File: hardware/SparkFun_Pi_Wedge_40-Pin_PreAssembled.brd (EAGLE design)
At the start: 82.5 x 65.5 mm, 17 parts

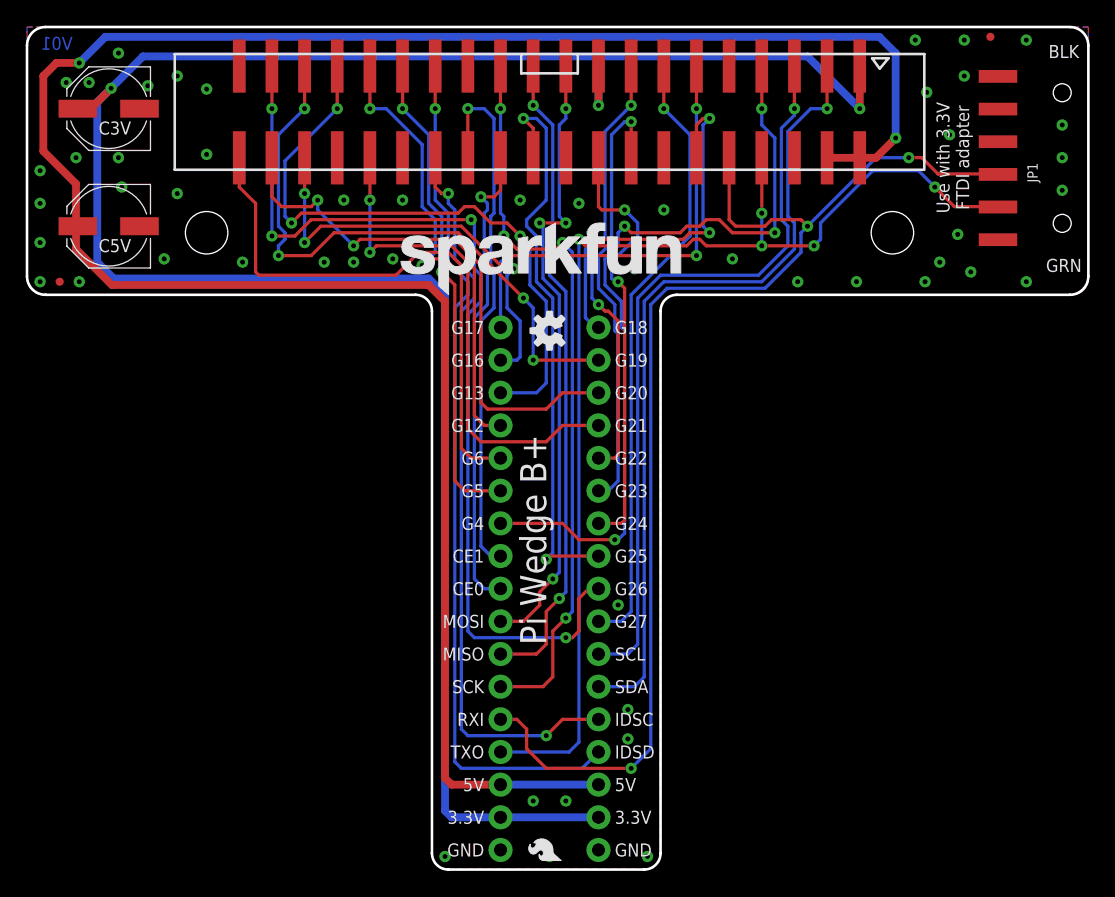
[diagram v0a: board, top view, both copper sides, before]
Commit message: Updates after group review.
A few silk touch-ups.
Renaming to "Pi Wedge 40-Pin".
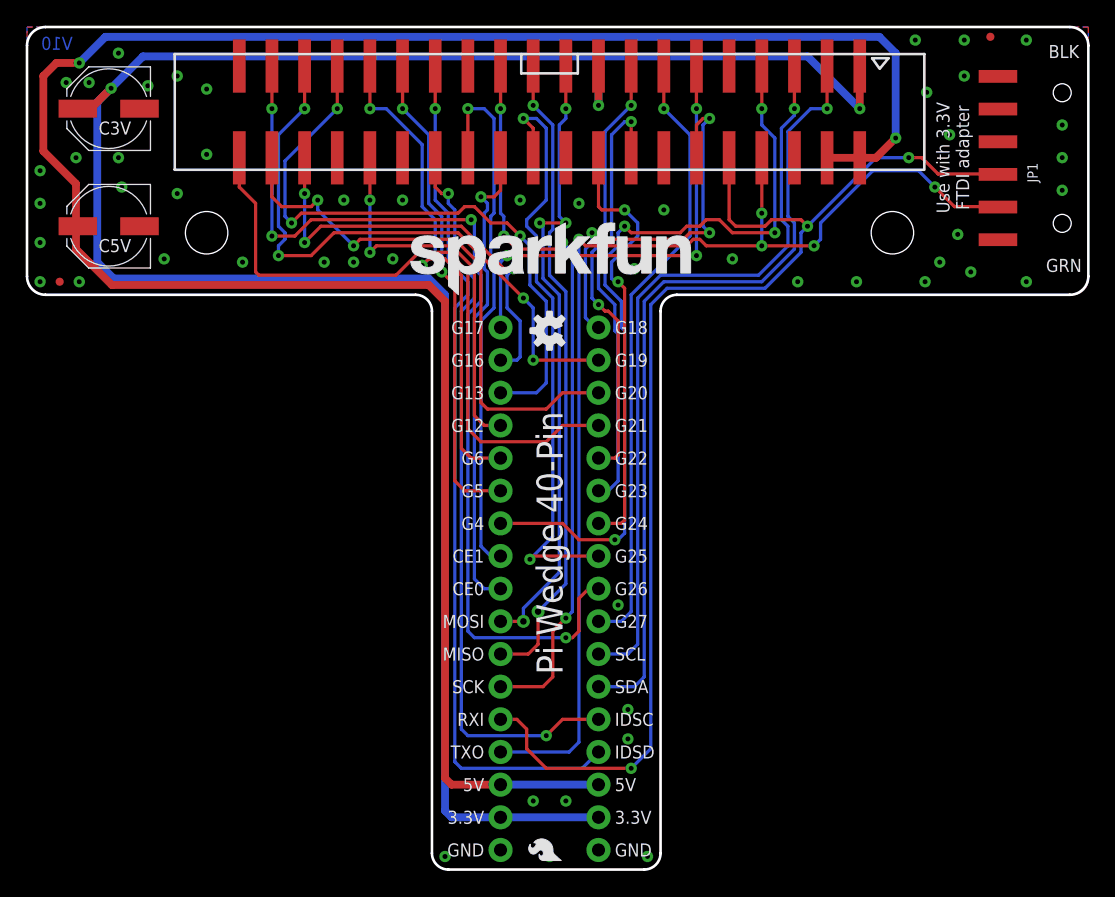
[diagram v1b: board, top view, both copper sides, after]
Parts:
- moved LOGO1 0.76 mm to (29.8, 44.7)
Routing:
- net GP25: track 44.9 -> 46.6 mm
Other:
- board text added: "Pi Wedge 40-Pin"
- board text added: "V10"
- board text removed: "Pi Wedge B+"
- board text removed: "V01"
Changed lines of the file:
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@@
 <wire x1="48.006" y1="0" x2="49.276" y2="1.27" width="0.2032" layer="20" curve="90"/>
 <wire x1="49.276" y1="1.27" x2="49.276" y2="43.434" width="0.2032" layer="20"/>
-<text x="3.556" y="63.754" size="1.016" layer="16" font="vector" ratio="20" rot="SMR0">V01</text>
+<text x="3.556" y="63.754" size="1.016" layer="16" font="vector" ratio="20" rot="SMR0">V10</text>
 <text x="35.56" y="1.524" size="1.016" layer="21" font="vector" ratio="19" rot="SR0" align="center-right">GND</text>
-<text x="40.386" y="25.654" size="2.032" layer="21" font="vector" ratio="19" rot="SR90" align="bottom-center">Pi Wedge B+</text>
+<text x="40.64" y="25.4" size="2.032" layer="21" font="vector" ratio="19" rot="SR90" align="center">Pi Wedge 40-Pin</text>
 <text x="45.72" y="16.764" size="1.016" layer="21" font="vector" ratio="19" rot="SR0" align="center-left">SCL</text>
 <text x="45.72" y="14.224" size="1.016" layer="21" font="vector" ratio="19" rot="SR0" align="center-left">SDA</text>
@@
 <text x="88.9" y="33.02" size="1.778" layer="47" font="vector" ratio="15">2x 0.13" holes
 Clear 4-40 screws</text>
+<text x="40.64" y="25.4" size="2.032" layer="22" font="vector" ratio="19" rot="SMR90" align="center">Pi Wedge 40-Pin</text>
+<text x="80.645" y="46.482" size="1.016" layer="22" font="vector" ratio="19" rot="SMR0" align="bottom-center">GRN</text>
+<text x="80.645" y="63.119" size="1.016" layer="22" font="vector" ratio="19" rot="SMR0" align="bottom-center">BLK</text>
+<text x="78.74" y="55.372" size="1.016" layer="22" font="vector" ratio="19" rot="SMR270" align="bottom-center">Use with 3.3V
+FTDI adapter</text>
 </plain>
 <attributes>
@@
 </element>
 <element name="FRAME2" library="SparkFun-Aesthetics" package="CREATIVE_COMMONS" value="FRAME-LETTER" x="19.558" y="-17.78"/>
-<element name="LOGO1" library="SparkFun-Aesthetics" package="SFE_LOGO_NAME_.2" value="SFE_LOGO_NAME.2_INCH" x="29.083" y="44.704"/>
+<element name="LOGO1" library="SparkFun-Aesthetics" package="SFE_LOGO_NAME_.2" value="SFE_LOGO_NAME.2_INCH" x="29.845" y="44.704"/>
 <element name="STANDOFF1" library="SparkFun-Electromechanical" package="STAND-OFF" value="STAND-OFF" x="13.97" y="49.53"/>
 <element name="STANDOFF2" library="SparkFun-Electromechanical" package="STAND-OFF" value="STAND-OFF" x="67.31" y="49.53"/>
@@
 <contactref element="JP4" pad="10"/>
 <contactref element="JP2" pad="22"/>
-<wire x1="44.45" y1="24.384" x2="40.64" y2="24.384" width="0.254" layer="1"/>
-<wire x1="40.64" y1="24.384" x2="40.386" y2="24.13" width="0.254" layer="1"/>
-<via x="40.386" y="24.13" extent="1-16" drill="0.381"/>
-<wire x1="40.386" y1="24.13" x2="40.894" y2="24.638" width="0.254" layer="16"/>
-<wire x1="40.894" y1="24.638" x2="40.894" y2="44.45" width="0.254" layer="16"/>
+<wire x1="44.45" y1="24.384" x2="39.37" y2="24.384" width="0.254" layer="1"/>
+<wire x1="39.37" y1="24.384" x2="39.116" y2="24.13" width="0.254" layer="1"/>
+<via x="39.116" y="24.13" extent="1-16" drill="0.381"/>
+<wire x1="39.116" y1="24.13" x2="40.894" y2="25.908" width="0.254" layer="16"/>
+<wire x1="40.894" y1="25.908" x2="40.894" y2="44.45" width="0.254" layer="16"/>
 <wire x1="40.894" y1="44.45" x2="39.624" y2="45.72" width="0.254" layer="16"/>
 <wire x1="39.624" y1="49.276" x2="38.862" y2="50.038" width="0.254" layer="16"/>
@@
 <contactref element="JP2" pad="21"/>
 <contactref element="JP3" pad="7"/>
-<wire x1="36.83" y1="16.764" x2="39.624" y2="16.764" width="0.254" layer="1"/>
-<wire x1="39.624" y1="16.764" x2="40.386" y2="17.526" width="0.254" layer="1"/>
-<wire x1="40.386" y1="17.526" x2="40.386" y2="20.066" width="0.254" layer="1"/>
-<wire x1="40.386" y1="20.066" x2="41.402" y2="21.082" width="0.254" layer="1"/>
-<via x="41.402" y="21.082" extent="1-16" drill="0.381"/>
-<wire x1="41.402" y1="21.082" x2="41.91" y2="21.59" width="0.254" layer="16"/>
-<wire x1="41.91" y1="21.59" x2="41.91" y2="44.958" width="0.254" layer="16"/>
+<wire x1="36.83" y1="16.764" x2="38.989" y2="16.764" width="0.254" layer="1"/>
+<wire x1="38.989" y1="16.764" x2="39.751" y2="17.526" width="0.254" layer="1"/>
+<wire x1="39.751" y1="17.526" x2="39.751" y2="20.066" width="0.254" layer="1"/>
+<wire x1="39.751" y1="20.066" x2="41.91" y2="22.225" width="0.254" layer="16"/>
+<wire x1="41.91" y1="22.225" x2="41.91" y2="44.958" width="0.254" layer="16"/>
 <wire x1="41.91" y1="44.958" x2="40.64" y2="46.228" width="0.254" layer="16"/>
 <wire x1="40.64" y1="49.53" x2="40.894" y2="49.784" width="0.254" layer="16"/>
@@
 <via x="39.37" y="59.436" extent="1-16" drill="0.381"/>
 <wire x1="39.37" y1="59.436" x2="40.894" y2="57.912" width="0.254" layer="16"/>
+<via x="39.751" y="20.066" extent="1-16" drill="0.508"/>
 </signal>
 <signal name="MOSI">
@@
 <contactref element="JP3" pad="8"/>
 <wire x1="36.83" y1="19.304" x2="38.608" y2="19.304" width="0.254" layer="1"/>
-<wire x1="38.608" y1="19.304" x2="39.878" y2="20.574" width="0.254" layer="1"/>
-<wire x1="39.878" y1="20.574" x2="39.878" y2="21.59" width="0.254" layer="1"/>
-<wire x1="39.878" y1="21.59" x2="40.894" y2="22.606" width="0.254" layer="1"/>
-<via x="40.894" y="22.606" extent="1-16" drill="0.381"/>
-<wire x1="40.894" y1="22.606" x2="41.402" y2="23.114" width="0.254" layer="16"/>
+<wire x1="38.608" y1="19.304" x2="38.608" y2="20.32" width="0.254" layer="16"/>
+<wire x1="38.608" y1="20.32" x2="41.402" y2="23.114" width="0.254" layer="16"/>
 <wire x1="41.402" y1="23.114" x2="41.402" y2="44.704" width="0.254" layer="16"/>
 <wire x1="41.402" y1="44.704" x2="40.132" y2="45.974" width="0.254" layer="16"/>
@@
 <wire x1="41.91" y1="58.42" x2="41.402" y2="57.912" width="0.254" layer="16"/>
 <wire x1="41.91" y1="59.182" x2="41.91" y2="58.42" width="0.254" layer="16"/>
+<via x="38.608" y="19.304" extent="1-16" drill="0.508"/>
 </signal>
 <signal name="CE0">

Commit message: Updates after checklist review.
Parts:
- JP2: value RASPBERRYPI-B+-GPIO-SMT -> RASPBERRYPI-40-PIN-GPIO-SMT
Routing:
- net 5V: track 175.5 -> 181.2 mm
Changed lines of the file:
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@@
 <setting verticaltext="up"/>
 </settings>
-<grid distance="0.05" unitdist="inch" unit="inch" style="lines" multiple="1" display="yes" altdistance="0.005" altunitdist="inch" altunit="inch"/>
+<grid distance="0.1" unitdist="inch" unit="inch" style="lines" multiple="1" display="yes" altdistance="0.01" altunitdist="inch" altunit="inch"/>
 <layers>
 <layer number="1" name="Top" color="4" fill="1" visible="yes" active="yes"/>
@@
 <layer number="37" name="tTest" color="7" fill="1" visible="no" active="yes"/>
 <layer number="38" name="bTest" color="7" fill="1" visible="no" active="yes"/>
-<layer number="39" name="tKeepout" color="4" fill="11" visible="no" active="yes"/>
+<layer number="39" name="tKeepout" color="4" fill="11" visible="yes" active="yes"/>
 <layer number="40" name="bKeepout" color="1" fill="11" visible="no" active="yes"/>
 <layer number="41" name="tRestrict" color="4" fill="10" visible="no" active="yes"/>
@@
 </element>
 <element name="U$2" library="SparkFun-Aesthetics" package="BREADBOARD_SPACING" value="BREADBOARD_PATTERN" x="40.64" y="68.834"/>
-<element name="JP2" library="SparkFun-Boards" package="2X20-SHROUDED-SMT" value="RASPBERRYPI-B+-GPIO-SMT" x="40.64" y="58.928" rot="R270">
+<element name="JP2" library="SparkFun-Boards" package="2X20-SHROUDED-SMT" value="RASPBERRYPI-40-PIN-GPIO-SMT" x="40.64" y="58.928" rot="R270">
 <attribute name="PROD_ID" value="CONN-13143" x="40.64" y="58.928" size="1.778" layer="27" rot="R270" display="off"/>
 </element>
@@
 <via x="67.564" y="56.896" extent="1-16" drill="0.381"/>
 <wire x1="3.81" y1="50.038" x2="3.95" y2="50.038" width="0.6096" layer="1"/>
-<wire x1="62.23" y1="55.3593" x2="64.77" y2="55.3593" width="0.6096" layer="1"/>
+<wire x1="62.23" y1="55.3593" x2="62.23" y2="52.832" width="0.6096" layer="1"/>
+<wire x1="62.23" y1="52.832" x2="62.992" y2="52.07" width="0.6096" layer="1"/>
+<wire x1="62.992" y1="52.07" x2="64.008" y2="52.07" width="0.6096" layer="1"/>
+<wire x1="64.008" y1="52.07" x2="64.77" y2="52.832" width="0.6096" layer="1"/>
+<wire x1="64.77" y1="52.832" x2="64.77" y2="55.3593" width="0.6096" layer="1"/>
 <wire x1="64.77" y1="55.3593" x2="66.0273" y2="55.3593" width="0.6096" layer="1"/>
 <wire x1="66.0273" y1="55.3593" x2="67.564" y2="56.896" width="0.6096" layer="1"/>

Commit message: Updating caps values.
It had 47uf library parts (CAP-10547), but the schem incorrectly showed
10uf as the value.

Schem now reads 47uf.
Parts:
- C3V, C5V: value 10uf -> 47uf
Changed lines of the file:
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@@
 <setting verticaltext="up"/>
 </settings>
-<grid distance="0.1" unitdist="inch" unit="inch" style="lines" multiple="1" display="yes" altdistance="0.01" altunitdist="inch" altunit="inch"/>
+<grid distance="0.05" unitdist="inch" unit="inch" style="lines" multiple="1" display="yes" altdistance="0.005" altunitdist="inch" altunit="inch"/>
 <layers>
 <layer number="1" name="Top" color="4" fill="1" visible="yes" active="yes"/>
@@
 <layer number="37" name="tTest" color="7" fill="1" visible="no" active="yes"/>
 <layer number="38" name="bTest" color="7" fill="1" visible="no" active="yes"/>
-<layer number="39" name="tKeepout" color="4" fill="11" visible="yes" active="yes"/>
+<layer number="39" name="tKeepout" color="4" fill="11" visible="no" active="yes"/>
 <layer number="40" name="bKeepout" color="1" fill="11" visible="no" active="yes"/>
 <layer number="41" name="tRestrict" color="4" fill="10" visible="no" active="yes"/>
@@
 <element name="STANDOFF1" library="SparkFun-Electromechanical" package="STAND-OFF" value="STAND-OFF" x="13.97" y="49.53"/>
 <element name="STANDOFF2" library="SparkFun-Electromechanical" package="STAND-OFF" value="STAND-OFF" x="67.31" y="49.53"/>
-<element name="C5V" library="SparkFun-Capacitors" package="PANASONIC_D" value="10uf" x="6.35" y="50.038" rot="R180">
+<element name="C5V" library="SparkFun-Capacitors" package="PANASONIC_D" value="47uf" x="6.35" y="50.038" rot="R180">
 <attribute name="PROD_ID" value="CAP-10547" x="6.35" y="50.038" size="1.778" layer="27" rot="R180" display="off"/>
 </element>
-<element name="C3V" library="SparkFun-Capacitors" package="PANASONIC_D" value="10uf" x="6.35" y="59.182" rot="R180">
+<element name="C3V" library="SparkFun-Capacitors" package="PANASONIC_D" value="47uf" x="6.35" y="59.182" rot="R180">
 <attribute name="PROD_ID" value="CAP-10547" x="6.35" y="59.182" size="1.778" layer="27" rot="R180" display="off"/>
 </element>
